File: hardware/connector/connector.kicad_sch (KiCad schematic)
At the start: 18 parts, among them J2 Autosport, J3 Goldpin

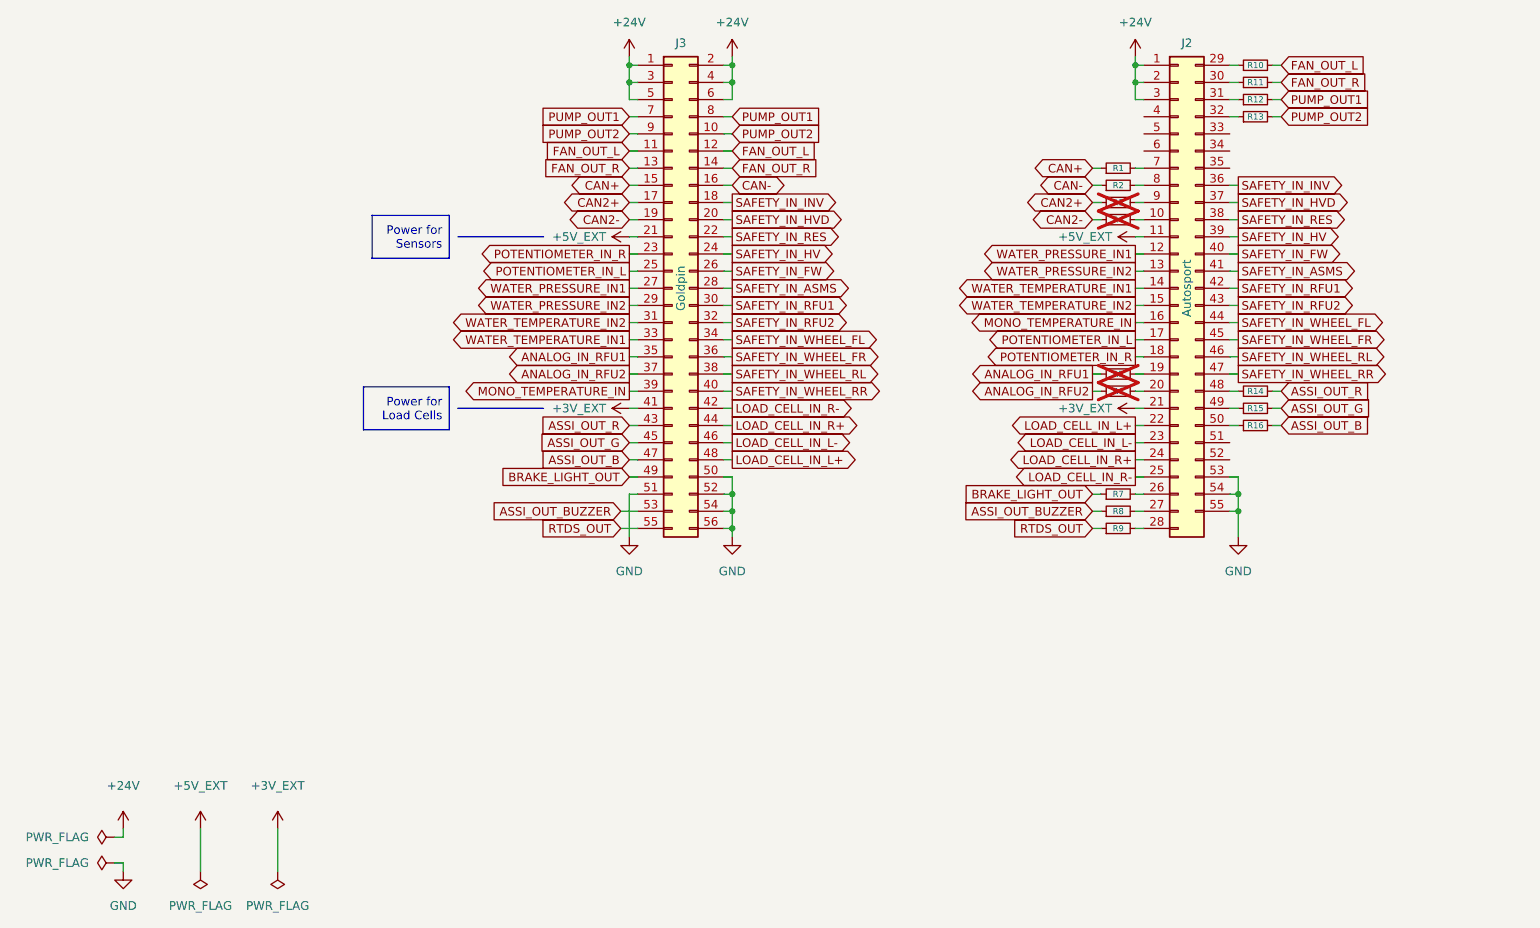
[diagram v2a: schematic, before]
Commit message: Route the tracks on the connector PCB
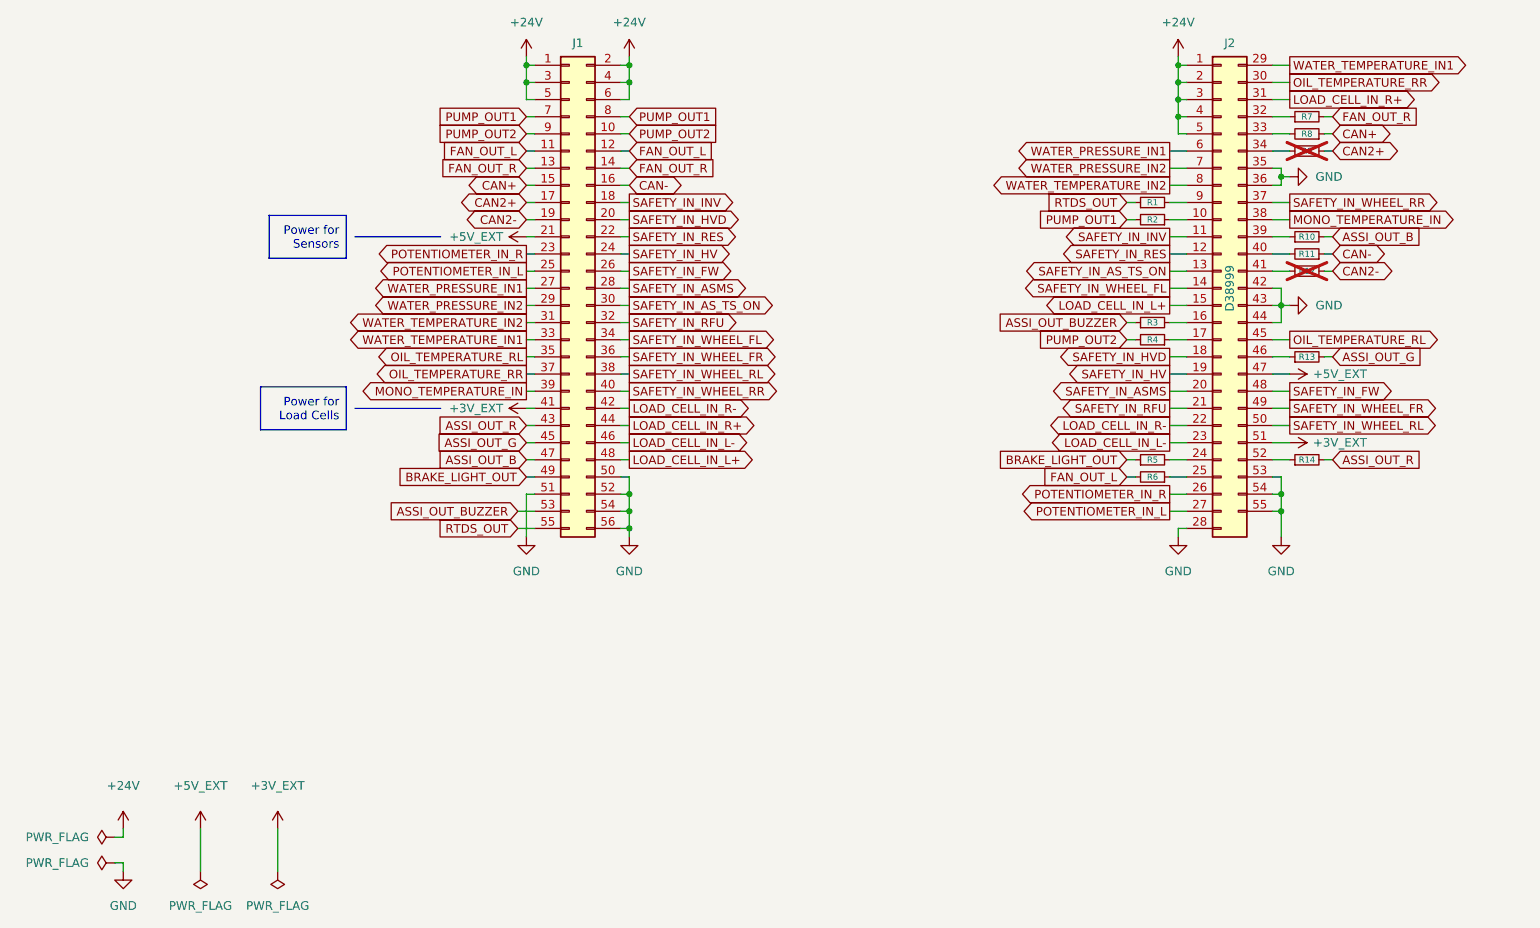
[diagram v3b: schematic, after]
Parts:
- removed J3: Goldpin, Connector_PinHeader_2.00mm:PinHeader_2x28_P2.00mm_Horizontal, symbol Connector_Generic:Conn_02x28_Odd_Even
- removed R5, R6: 0R, Resistor_SMD:R_0603_1608Metric, symbol Device:R_Small
- added J1: Conn_02x28_Top_Bottom, Local_Library:PinHeader_2x28_P2.00mm_Horizontal, symbol Connector_Generic:Conn_02x28_Odd_Even
- J2: value Autosport -> D38999; footprint Local_Library:AS022-55SN -> Local_Library:DTS20W17-35SN; symbol AS022-55SN:AS022-55SN -> DTS20W17-35SN:DTS20W17-35SN; Component AS022-55SN -> DTS20W17-35SN
- renumbered R9 to R1, R16 to R10, R2 to R11, R4 to R12, R15 to R13, R12 to R2, R8 to R3, R13 to R4, R7 to R5, R10 to R6, R11 to R7, R1 to R8, R3 to R9
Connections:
- net SAFETY_IN_RFU1 is gone; now on net GND: J2.42 (Pin_42)
- net SAFETY_IN_RFU2 is gone; now on net GND: J2.43 (Pin_43)
- net +24V: now also J2.4 (Pin_4), J2.5 (Pin_5), J1.1 (Pin_1), J1.2 (Pin_2), J1.3 (Pin_3), J1.4 (Pin_4), J1.5 (Pin_5), J1.6 (Pin_6)
- net +3V_EXT: now also J2.51 (Pin_51), J1.41 (Pin_41); no longer J2.21 (Pin_21)
- net +5V_EXT: now also J2.47 (Pin_47), J1.21 (Pin_21); no longer J2.11 (Pin_11)
- net ASSI_OUT_B: now also J1.47 (Pin_47)
- net ASSI_OUT_BUZZER: now also J1.53 (Pin_53)
- net ASSI_OUT_G: now also J1.45 (Pin_45)
- net ASSI_OUT_R: now also J1.43 (Pin_43)
- net BRAKE_LIGHT_OUT: now also J1.49 (Pin_49)
- net CAN+: now also J1.15 (Pin_15)
- net CAN-: now also J1.16 (Pin_16)
- net CAN2+: now also J1.17 (Pin_17)
- net CAN2-: now also J1.19 (Pin_19)
- net FAN_OUT_L: now also J1.11 (Pin_11), J1.12 (Pin_12)
- net FAN_OUT_R: now also J1.13 (Pin_13), J1.14 (Pin_14)
- net GND: now also J2.28 (Pin_28), J2.35 (Pin_35), J2.36 (Pin_36), J2.44 (Pin_44), J1.50 (Pin_50), J1.51 (Pin_51), J1.52 (Pin_52), J1.54 (Pin_54), J1.56 (Pin_56)
- net LOAD_CELL_IN_L+: now also J2.15 (Pin_15), J1.48 (Pin_48); no longer J2.22 (Pin_22)
- net LOAD_CELL_IN_L-: now also J1.46 (Pin_46)
- net LOAD_CELL_IN_R+: now also J2.31 (Pin_31), J1.44 (Pin_44); no longer J2.24 (Pin_24)
- net LOAD_CELL_IN_R-: now also J2.22 (Pin_22), J1.42 (Pin_42); no longer J2.25 (Pin_25)
- net MONO_TEMPERATURE_IN: now also J2.38 (Pin_38), J1.39 (Pin_39); no longer J2.16 (Pin_16)
- net POTENTIOMETER_IN_L: now also J2.27 (Pin_27), J1.25 (Pin_25); no longer J2.17 (Pin_17)
- net POTENTIOMETER_IN_R: now also J2.26 (Pin_26), J1.23 (Pin_23); no longer J2.18 (Pin_18)
- net PUMP_OUT1: now also J1.7 (Pin_7), J1.8 (Pin_8)
- net PUMP_OUT2: now also J1.10 (Pin_10), J1.9 (Pin_9)
- net RTDS_OUT: now also J1.55 (Pin_55)
- net SAFETY_IN_ASMS: now also J2.20 (Pin_20), J1.28 (Pin_28); no longer J2.41 (Pin_41)
- net SAFETY_IN_FW: now also J2.48 (Pin_48), J1.26 (Pin_26); no longer J2.40 (Pin_40)
- net SAFETY_IN_HV: now also J2.19 (Pin_19), J1.24 (Pin_24); no longer J2.39 (Pin_39)
- net SAFETY_IN_HVD: now also J2.18 (Pin_18), J1.20 (Pin_20); no longer J2.37 (Pin_37)
- net SAFETY_IN_INV: now also J2.11 (Pin_11), J1.18 (Pin_18); no longer J2.36 (Pin_36)
- net SAFETY_IN_RES: now also J2.12 (Pin_12), J1.22 (Pin_22); no longer J2.38 (Pin_38)
- net SAFETY_IN_WHEEL_FL: now also J2.14 (Pin_14), J1.34 (Pin_34); no longer J2.44 (Pin_44)
- net SAFETY_IN_WHEEL_FR: now also J2.49 (Pin_49), J1.36 (Pin_36); no longer J2.45 (Pin_45)
- net SAFETY_IN_WHEEL_RL: now also J2.50 (Pin_50), J1.38 (Pin_38); no longer J2.46 (Pin_46)
- net SAFETY_IN_WHEEL_RR: now also J2.37 (Pin_37), J1.40 (Pin_40); no longer J2.47 (Pin_47)
- net WATER_PRESSURE_IN1: now also J2.6 (Pin_6), J1.27 (Pin_27); no longer J2.12 (Pin_12)
- net WATER_PRESSURE_IN2: now also J2.7 (Pin_7), J1.29 (Pin_29); no longer J2.13 (Pin_13)
- net WATER_TEMPERATURE_IN1: now also J2.29 (Pin_29), J1.33 (Pin_33); no longer J2.14 (Pin_14)
- net WATER_TEMPERATURE_IN2: now also J2.8 (Pin_8), J1.31 (Pin_31); no longer J2.15 (Pin_15)
- net at R1.2: now also J2.9 (Pin_9); no longer J2.28 (Pin_28)
- net at R3.2: now also J2.16 (Pin_16); no longer J2.27 (Pin_27)
- net at R5.2: now also J2.24 (Pin_24); no longer J2.26 (Pin_26)
- net at R2.1: now also J2.10 (Pin_10); no longer J2.31 (Pin_31)
- net at R4.1: now also J2.17 (Pin_17); no longer J2.32 (Pin_32)
- net at R12.2: now also J2.41 (Pin_41); no longer J2.10 (Pin_10)
- net at R8.2: now also J2.33 (Pin_33); no longer J2.7 (Pin_7)
- net at R7.1: now also J2.32 (Pin_32); no longer J2.30 (Pin_30)
- net at R13.1: now also J2.46 (Pin_46); no longer J2.49 (Pin_49)
- net at R9.2: now also J2.34 (Pin_34); no longer J2.9 (Pin_9)
- net at R11.2: now also J2.40 (Pin_40); no longer J2.8 (Pin_8)
- net at R14.1: now also J2.52 (Pin_52); no longer J2.48 (Pin_48)
- net at R10.1: now also J2.39 (Pin_39); no longer J2.50 (Pin_50)
- net at R6.1: now also J2.25 (Pin_25); no longer J2.29 (Pin_29)
- new net OIL_TEMPERATURE_RL: J1.35 (Pin_35), J2.45 (Pin_45)
- new net OIL_TEMPERATURE_RR: J1.37 (Pin_37), J2.30 (Pin_30)
- new net SAFETY_IN_AS_TS_ON: J1.30 (Pin_30), J2.13 (Pin_13)
- new net SAFETY_IN_RFU: J1.32 (Pin_32), J2.21 (Pin_21)
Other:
- moved on the sheet: J2, R1, R10, R11, R12, R13, R14, R2, R3, R4, R5, R6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

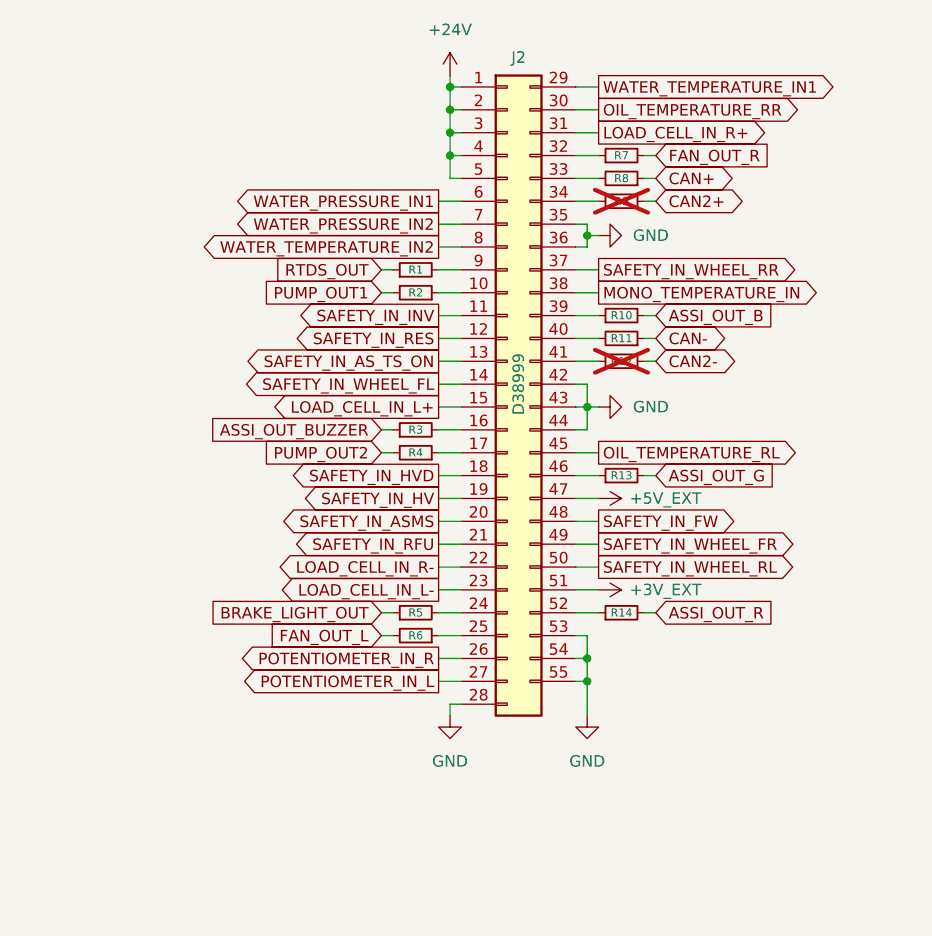
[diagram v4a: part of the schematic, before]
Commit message: Fix connector wiring
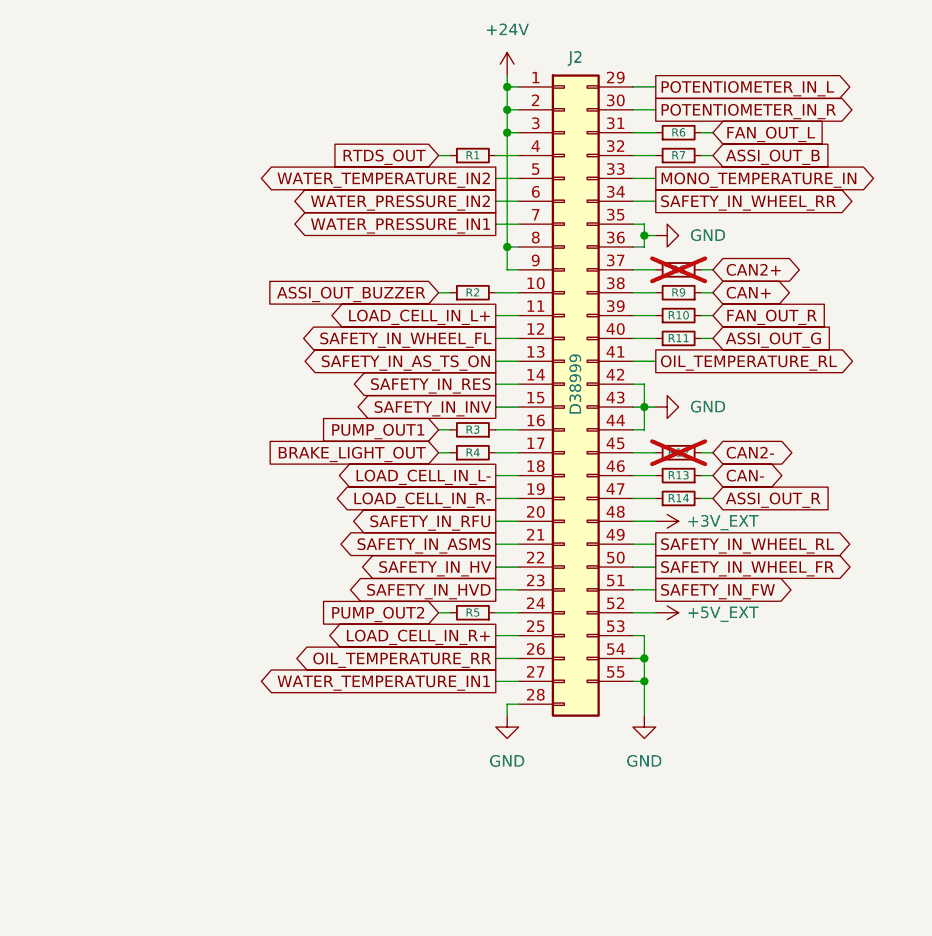
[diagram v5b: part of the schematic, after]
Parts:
- renumbered R7 to R10, R13 to R11, R11 to R13, R3 to R2, R2 to R3, R5 to R4, R4 to R5, R10 to R7, R9 to R8, R8 to R9
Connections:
- net +24V: now also J2.8 (Pin_8), J2.9 (Pin_9); no longer J2.4 (Pin_4), J2.5 (Pin_5)
- net +3V_EXT: now also J2.48 (Pin_48); no longer J2.51 (Pin_51)
- net +5V_EXT: now also J2.52 (Pin_52); no longer J2.47 (Pin_47)
- net LOAD_CELL_IN_L+: now also J2.11 (Pin_11); no longer J2.15 (Pin_15)
- net LOAD_CELL_IN_L-: now also J2.18 (Pin_18); no longer J2.23 (Pin_23)
- net LOAD_CELL_IN_R+: now also J2.25 (Pin_25); no longer J2.31 (Pin_31)
- net LOAD_CELL_IN_R-: now also J2.19 (Pin_19); no longer J2.22 (Pin_22)
- net MONO_TEMPERATURE_IN: now also J2.33 (Pin_33); no longer J2.38 (Pin_38)
- net OIL_TEMPERATURE_RL: now also J2.41 (Pin_41); no longer J2.45 (Pin_45)
- net OIL_TEMPERATURE_RR: now also J2.26 (Pin_26); no longer J2.30 (Pin_30)
- net POTENTIOMETER_IN_L: now also J2.29 (Pin_29); no longer J2.27 (Pin_27)
- net POTENTIOMETER_IN_R: now also J2.30 (Pin_30); no longer J2.26 (Pin_26)
- net SAFETY_IN_ASMS: now also J2.21 (Pin_21); no longer J2.20 (Pin_20)
- net SAFETY_IN_FW: now also J2.51 (Pin_51); no longer J2.48 (Pin_48)
- net SAFETY_IN_HV: now also J2.22 (Pin_22); no longer J2.19 (Pin_19)
- net SAFETY_IN_HVD: now also J2.23 (Pin_23); no longer J2.18 (Pin_18)
- net SAFETY_IN_INV: now also J2.15 (Pin_15); no longer J2.11 (Pin_11)
- net SAFETY_IN_RES: now also J2.14 (Pin_14); no longer J2.12 (Pin_12)
- net SAFETY_IN_RFU: now also J2.20 (Pin_20); no longer J2.21 (Pin_21)
- net SAFETY_IN_WHEEL_FL: now also J2.12 (Pin_12); no longer J2.14 (Pin_14)
- net SAFETY_IN_WHEEL_FR: now also J2.50 (Pin_50); no longer J2.49 (Pin_49)
- net SAFETY_IN_WHEEL_RL: now also J2.49 (Pin_49); no longer J2.50 (Pin_50)
- net SAFETY_IN_WHEEL_RR: now also J2.34 (Pin_34); no longer J2.37 (Pin_37)
- net WATER_PRESSURE_IN1: now also J2.7 (Pin_7); no longer J2.6 (Pin_6)
- net WATER_PRESSURE_IN2: now also J2.6 (Pin_6); no longer J2.7 (Pin_7)
- net WATER_TEMPERATURE_IN1: now also J2.27 (Pin_27); no longer J2.29 (Pin_29)
- net WATER_TEMPERATURE_IN2: now also J2.5 (Pin_5); no longer J2.8 (Pin_8)
- net at R1.2: now also J2.4 (Pin_4); no longer J2.9 (Pin_9)
- net at R2.2: now also J2.10 (Pin_10); no longer J2.16 (Pin_16)
- net at R4.2: now also J2.17 (Pin_17); no longer J2.24 (Pin_24)
- net at R3.1: now also J2.16 (Pin_16); no longer J2.10 (Pin_10)
- net at R5.1: now also J2.24 (Pin_24); no longer J2.17 (Pin_17)
- net at R12.2: now also J2.45 (Pin_45); no longer J2.41 (Pin_41)
- net at R9.2: now also J2.38 (Pin_38); no longer J2.33 (Pin_33)
- net at R10.1: now also J2.39 (Pin_39); no longer J2.32 (Pin_32)
- net at R11.1: now also J2.40 (Pin_40); no longer J2.46 (Pin_46)
- net at R8.2: now also J2.37 (Pin_37); no longer J2.34 (Pin_34)
- net at R13.2: now also J2.46 (Pin_46); no longer J2.40 (Pin_40)
- net at R14.1: now also J2.47 (Pin_47); no longer J2.52 (Pin_52)
- net at R7.1: now also J2.32 (Pin_32); no longer J2.39 (Pin_39)
- net at R6.1: now also J2.31 (Pin_31); no longer J2.25 (Pin_25)
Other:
- moved on the sheet: J2, R1, R10, R11, R12, R13, R14, R2, R3, R4, R5, R6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
